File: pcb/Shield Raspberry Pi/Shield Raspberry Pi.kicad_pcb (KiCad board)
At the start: 2 copper layers, 65 x 56 mm, 58 parts, among them J1 Conn_01x03, J10 Conn_01x02, J2 Conn_01x03, J3 Conn_01x03, J4 Jack-DC, J5 Raspberry_Pi_2_3, J6 Conn_01x02, J7 Conn_01x02, J8 Conn_01x02, J9 Conn_01x02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

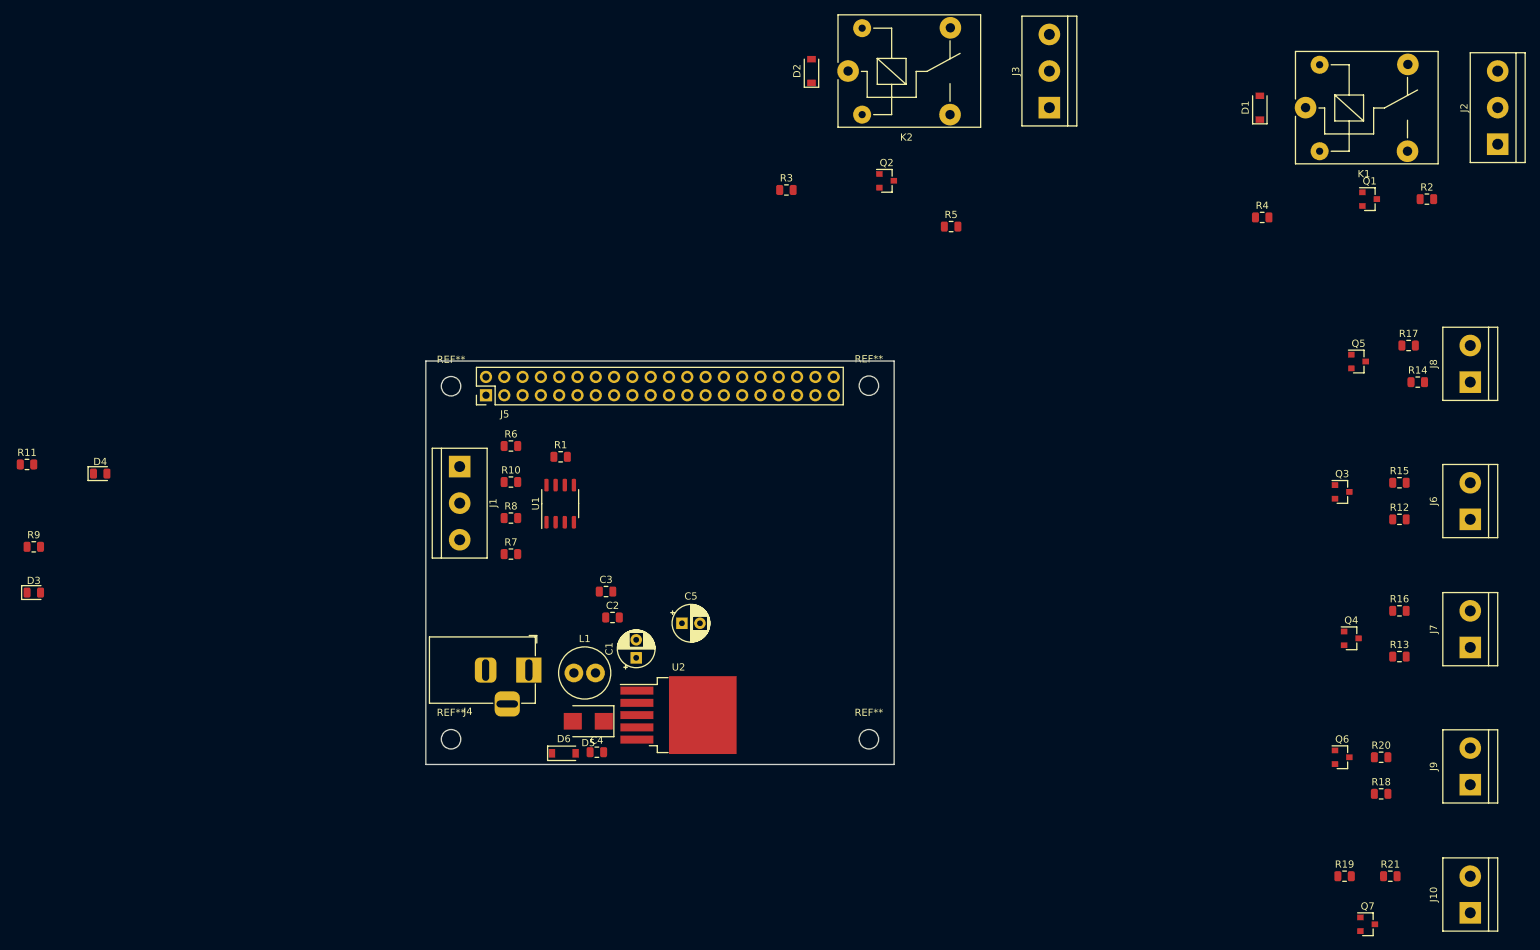
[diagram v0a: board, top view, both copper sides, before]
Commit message: Falta el ruteo, todo el resto está listo
Se completó el modelado 3D, se ubicaron todos los componentes, solo falta el ruteo
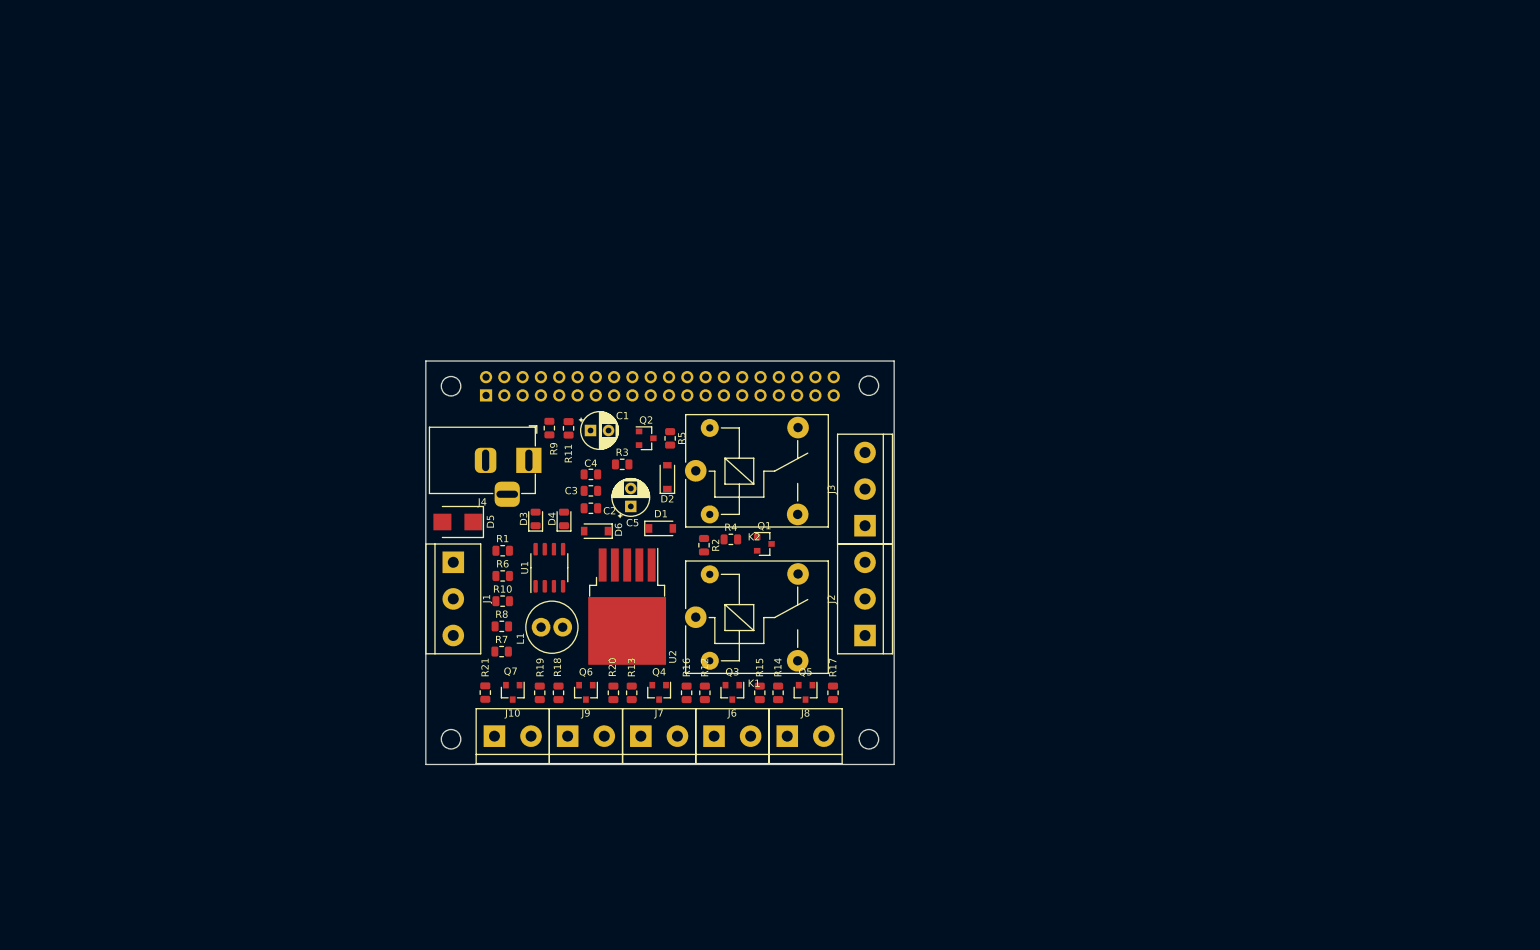
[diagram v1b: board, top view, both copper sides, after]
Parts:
-  : renamed from REF** (x4)
- C1: value 47u -> (none)
- C2: value 1u -> (none)
- C3: value 100n -> (none)
- C4: value 10n -> (none)
- C5: value 100u -> (none)
- D1, D2, D6: value 1N5819HW-7-F -> (none)
- D3: value LED1 -> (none)
- D4: value LED2 -> (none)
- D5: value SMBJ5.0A -> (none)
- J1, J2, J3: value Conn_01x03 -> (none)
- J10, J6, J7, J8, J9: value Conn_01x02 -> (none)
- J4: value Jack-DC -> (none)
- J5: value Raspberry_Pi_2_3 -> (none); moved to B.Cu
- K1, K2: value SANYOU RELAY -> (none)
- L1: value 33uHy -> (none)
- Q1, Q2, Q3, Q4, Q5, Q6, Q7: value 2N7002 -> (none)
- R1, R11, R4, R5, R9: value 120 -> (none)
- R10, R12, R13, R14, R15, R16, R17, R18, R19, R2, R20, R21, R3, R6, R7, R8: value 10k -> (none)
- U1: value MAX485E -> (none)
- U2: value LM2596 5.0 -> (none)
- moved J10 137.6 mm to (132.5, 124.1), turned to 0 degrees
- moved R21 128.2 mm to (131.3, 118.0), turned to 270 degrees
- moved J9 125.5 mm to (142.7, 124.1), turned to 0 degrees
- moved Q7 123.0 mm to (135.1, 118.0), turned to 270 degrees
- moved J7 115.8 mm to (152.8, 124.1), turned to 0 degrees
- moved R18 115.0 mm to (141.4, 118.1), turned to 270 degrees
- moved R19 114.6 mm to (138.8, 118.1), turned to 90 degrees
- moved R2 111.3 mm to (161.6, 97.6), turned to 270 degrees
- moved J2 111.2 mm to (184.0, 110.1)
- moved K1 110.3 mm to (160.5, 107.6)
- moved J6 109.2 mm to (163.0, 124.1), turned to 0 degrees
- moved R20 106.9 mm to (149.0, 118.1), turned to 270 degrees
- moved J8 106.8 mm to (173.2, 124.1), turned to 0 degrees
- moved R13 106.7 mm to (151.6, 118.1), turned to 270 degrees
- moved Q6 105.4 mm to (145.2, 118.0), turned to 270 degrees
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
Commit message: Add files via upload
Version completamente ruteada, faltan solo algunas leyendas
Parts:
- added  : , Symbol:ESD-Logo_6.6x6mm_SilkScreen, B.Cu at (184.1, 116.8)
- added  : , Symbol:Symbol_Barrel_Polarity, B.Cu at (125.8, 85.7)
- added  : , Symbol:EJ TECH 18X11, B.Cu at (143.8, 99.2)
- added  : , Symbol:EJ TECH 8X5.5, F.Cu at (126.6, 117.5)
- added D7: D, Diode_SMD:D_SMB, F.Cu at (142.7, 87.5)
- C1: value (none) -> 47u
- C2: value (none) -> 1u
- C3: value (none) -> 100n
- C4: value (none) -> 10n
- C5: value (none) -> 100u
- D1, D2, D6: value (none) -> 1N5819HW-7-F
- D3: value (none) -> LED1
- D4: value (none) -> LED2
- D5: value (none) -> SMBJ5.0A
- J1, J2, J3: value (none) -> Conn_01x03
- J10, J6, J7, J8, J9: value (none) -> Conn_01x02
- J4: value (none) -> Jack-DC
- J5: value (none) -> Raspberry_Pi_2_3
- K1, K2: value (none) -> SANYOU RELAY
- L1: value (none) -> 33uHy
- Q1, Q2, Q3, Q4, Q5, Q6, Q7: value (none) -> 2N7002
- R1, R11, R4, R5, R9: value (none) -> 120
- R10, R12, R13, R14, R15, R16, R17, R18, R19, R2, R20, R21, R3, R6, R7, R8: value (none) -> 10k
- U1: value (none) -> MAX485E
- U2: value (none) -> LM2596 5.0
- moved C3 8.07 mm to (144.8, 98.0)
- moved C4 2.16 mm to (147.1, 89.5), turned to 90 degrees
- moved C2 0.28 mm to (146.2, 92.4)
- moved R10 0.12 mm to (133.5, 105.3)
- moved R6 0.12 mm to (133.5, 101.8)
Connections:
- J4 pad 1: Net-(C1-Pad1) -> Net-(D7-Pad2)
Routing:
- net GND: track 0.00 -> 331.1 mm, vias 0 -> 4
- net +5V: track 0.00 -> 216.0 mm, vias 0 -> 3
- net +3V3: track 0.00 -> 149.9 mm, vias 0 -> 2
- net GP26: track 0.00 -> 81.1 mm, vias 0 -> 2
- net GP22: track 0.00 -> 64.9 mm, vias 0 -> 2
- net Net-(J5-Pad31): track 0.00 -> 60.4 mm, vias 0 -> 4
- net Net-(J5-Pad33): track 0.00 -> 59.1 mm, vias 0 -> 6
- net RE: track 0.00 -> 58.4 mm, vias 0 -> 1
- net DE: track 0.00 -> 55.4 mm, vias 0 -> 1
- net Net-(J5-Pad29): track 0.00 -> 54.6 mm, vias 0 -> 2
- net TX: track 0.00 -> 46.9 mm, vias 0 -> 3
- net RX: track 0.00 -> 44.7 mm, vias 0 -> 2
- net Net-(C1-Pad1): track 0.00 -> 36.8 mm, vias 0 -> 2
- net Net-(J1-Pad2): track 0.00 -> 29.6 mm
- net Net-(D6-Pad1): track 0.00 -> 28.0 mm, vias 0 -> 1
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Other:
- board size 65 x 56 mm -> 67.4 x 57.2 mm
- rule pad_to_mask_clearance: 0.051 -> 0.1
- rule via_min_drill: 0.3 -> 0.25
- rule via_min_size: 0.4 -> 0.55
- board text added: "+"
- board text added: "-"
- board text added: "Designed by Dario El Jatib"
- board text added: "GND"
- board text added: "GP13"
- board text added: "GP22"
- board text added: "GP26"
- board text added: "GP5"
- board text added: "GP6"

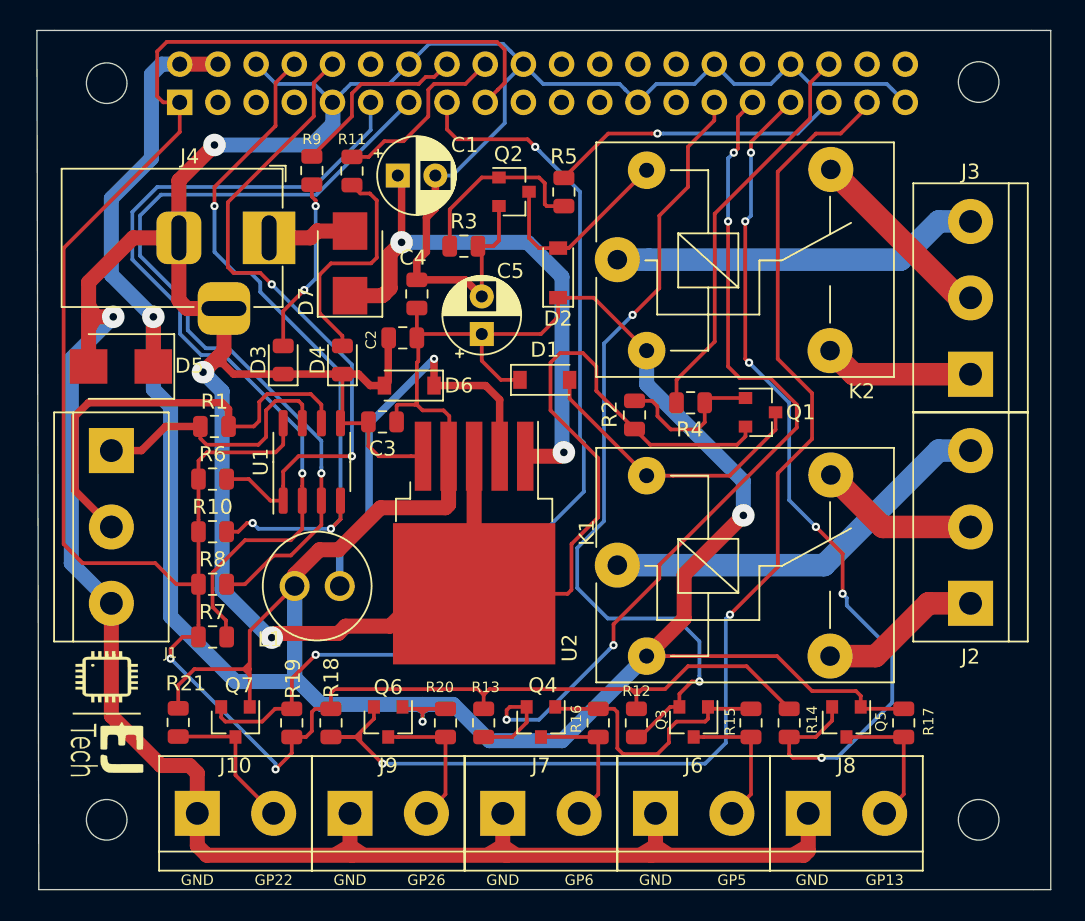
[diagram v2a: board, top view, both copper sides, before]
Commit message: Add files via upload
Proyecto terminado, tiene el ruteo, sin plano de masa, con todas las serigrafías
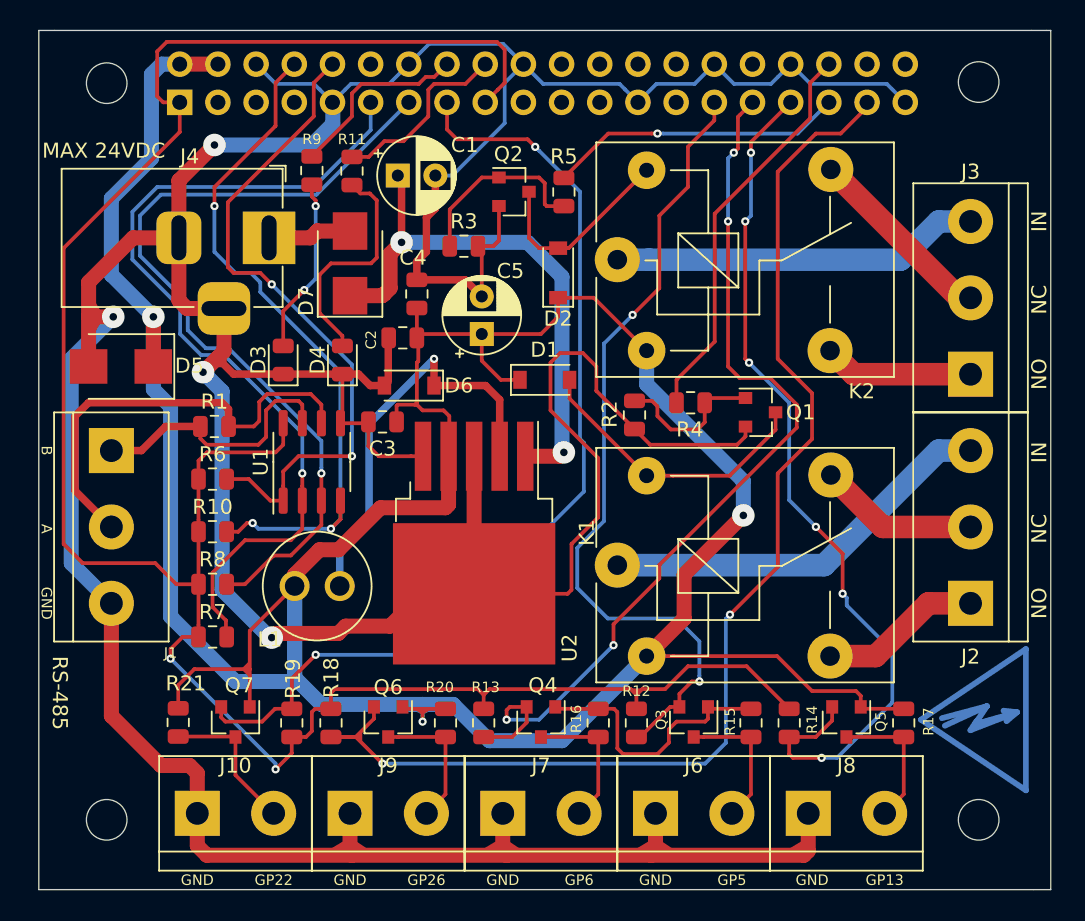
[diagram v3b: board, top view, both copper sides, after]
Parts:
- removed the   at (184.1, 116.8)
- removed the   at (143.8, 99.2)
- removed the   at (126.6, 117.5)
- added  : , Symbol:Symbol_HighVoltage_Type2_CopperTop_VerySmall, B.Cu at (184.8, 117.8)
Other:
- board size 67.4 x 57.2 mm -> 67.3 x 57.2 mm
- board text added: "5V Adapted"
- board text added: "A"
- board text added: "B"
- board text added: "IN"
- board text added: "MAX 24VDC"
- board text added: "NC"
- board text added: "NO"
- board text added: "RS-485"
- board text added: "Vin Adapted"
